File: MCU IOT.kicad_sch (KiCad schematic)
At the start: 0 parts

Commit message: Add IOT Part
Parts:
- added C?: 10nF, Capacitor_SMD:C_0603_1608Metric_Pad1.08x0.95mm_HandSolder, symbol Device:C_Small
- added C? (x8): 100nF, Capacitor_SMD:C_0603_1608Metric_Pad1.08x0.95mm_HandSolder, symbol Device:C_Small
- added D? (x5): 3.3V, Package_TO_SOT_SMD:SOT-363_SC-70-6, symbol Power_Protection:PESD3V3L5UY
- added D? (x4): 3.3V, Diode_SMD:D_SOD-123F, symbol Device:D_Zener_Small
- added D?: 5V, Diode_SMD:D_SMB, symbol Device:D_Zener_Small
- added F?: 1.75A, Fuse:Fuse_0603_1608Metric, symbol Device:Fuse_Small
- added J? (x3): *, Connector_JST:JST_PH_S6B-PH-SM4-TB_1x06-1MP_P2.00mm_Horizontal, symbol Connector_Generic_MountingPin:Conn_01x06_MountingPin
- added J?: *, Connector_USB:USB_B_Amphenol_MUSB-D511_Vertical_Rugged, symbol Connector:USB_B_Micro
- added J?: *, TerminalBlock_Phoenix:TerminalBlock_Phoenix_MPT-0,5-4-2.54_1x04_P2.54mm_Horizontal, symbol Connector:Screw_Terminal_01x04
- added J?: *, Connector_JST:JST_PH_S4B-PH-SM4-TB_1x04-1MP_P2.00mm_Horizontal, symbol Connector_Generic_MountingPin:Conn_01x04_MountingPin
- added J?: *, TerminalBlock_Phoenix:TerminalBlock_Phoenix_MPT-0,5-6-2.54_1x06_P2.54mm_Horizontal, symbol Connector:Screw_Terminal_01x06
- added R? (x3): 10k, Resistor_SMD:R_0603_1608Metric_Pad0.98x0.95mm_HandSolder, symbol Device:R_Small
- added R? (x4): 22R, Resistor_SMD:R_0805_2012Metric_Pad1.20x1.40mm_HandSolder, symbol Device:R_Small
- added R? (x3): 4.7k, Resistor_SMD:R_0603_1608Metric_Pad0.98x0.95mm_HandSolder, symbol Device:R_Small
- added R? (x2): 604R, Resistor_SMD:R_0603_1608Metric_Pad0.98x0.95mm_HandSolder, symbol Device:R_Small
- added R? (x2): 22R, Resistor_SMD:R_0603_1608Metric_Pad0.98x0.95mm_HandSolder, symbol Device:R_Small
- added SW? (x2): *, Button_Switch_SMD:SW_SPST_CK_RS282G05A3, symbol Switch:SW_Push
- added U?: TJA1042T-3, Package_SO:SOIC-8_3.9x4.9mm_P1.27mm, symbol Interface_CAN_LIN:TJA1042T-3
- added U?: *, P_MCU:XCVR_ESP32-C6-WROOM-1U-N8, symbol P_MCU:ESP32-C6-WROOM-1U-N4
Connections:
- new net: D?.5 (K4), J?.5 (Pin_5), R?.1
- new net: C?.1, R?.2, R?.2
- new net: R?.1, U?.10 (IO8)
- new net: F?.1, J?.1 (VBUS)
- new net: J?.2 (D-), R?.1
- new net: J?.3 (D+), R?.1
- new net: D?.3 (K2), J?.3 (Pin_3), R?.1
- new net: D?.6 (K5), J?.6 (Pin_6), R?.1
- new net: D?.4 (K3), J?.4 (Pin_4), R?.1
- new net +3.3V: C?.1, C?.1, C?.1, C?.1, C?.1, D?.1 (K1), J?.1 (Pin_1), J?.1 (Pin_1), J?.1 (Pin_1), J?.1 (Pin_1), R?.2, R?.2, R?.2, R?.2, U?.2 (3V3), U?.5 (VIO)
- new net +5V: C?.1, D?.1 (K), F?.2, J?.1 (Pin_1), R?.2, U?.3 (VCC)
- new net BOOT: C?.1, R?.1, SW?.1, U?.15 (IO9)
- new net CAN_H: J?.3 (Pin_3), R?.1, U?.7 (CANH)
- new net CAN_L: J?.4 (Pin_4), R?.1, U?.6 (CANL)
- new net EN: C?.1, R?.1, SW?.1, U?.3 (EN)
- new net ESP_CAN_RX: U?.21 (IO23), U?.4 (RXD)
- new net ESP_CAN_STB: U?.19 (IO21), U?.8 (STB)
- new net ESP_CAN_TX: U?.1 (TXD), U?.20 (IO22)
- new net ESP_I2C_SCL: J?.4 (Pin_4), R?.1, U?.5 (IO5)
- new net ESP_I2C_SDA: J?.3 (Pin_3), R?.1, U?.4 (IO4)
- new net ESP_PWM/ADC1: D?.1 (K), R?.2, U?.8 (IO0)
- new net ESP_PWM/ADC2: D?.1 (K), R?.2, U?.9 (IO1)
- new net ESP_PWM/ADC3: D?.1 (K), R?.2, U?.27 (IO2)
- new net ESP_PWM/ADC4: D?.1 (K), R?.2, U?.26 (IO3)
- new net ESP_SPARE1: U?.23 (IO15)
- new net ESP_SPARE2: U?.12 (IO11)
- new net ESP_SPARE3: U?.11 (IO10)
- new net ESP_SPI_CS0: J?.6 (Pin_6), U?.17 (IO19)
- new net ESP_SPI_CS1: J?.6 (Pin_6), U?.18 (IO20)
- new net ESP_SPI_MISO: J?.5 (Pin_5), J?.5 (Pin_5), U?.16 (IO18)
- new net ESP_SPI_MOSI: J?.4 (Pin_4), J?.4 (Pin_4), U?.7 (IO7)
- new net ESP_SPI_SCK: J?.3 (Pin_3), J?.3 (Pin_3), U?.6 (IO6)
- new net ESP_USB_D+: R?.1, R?.2, U?.14 (IO13)
- new net ESP_USB_D-: R?.2, U?.13 (IO12)
- new net GND: C?.2, C?.2, C?.2, C?.2, C?.2, C?.2, C?.2, C?.2, C?.2, D?.2 (A), D?.2 (A), D?.2 (A), D?.2 (A), D?.2 (A), D?.2 (A), J?.2 (Pin_2), J?.2 (Pin_2), J?.2 (Pin_2), J?.2 (Pin_2), J?.2 (Pin_2), J?.5 (GND), J?.MP (MountPin), J?.MP (MountPin), J?.MP (MountPin), J?.SH (Shield), R?.2, SW?.2, SW?.2, U?.1 (GND), U?.2 (GND), U?.28 (GND), U?.29_1 (GND), U?.29_2 (GND), U?.29_3 (GND), U?.29_4 (GND), U?.29_5 (GND), U?.29_6 (GND), U?.29_7 (GND), U?.29_8 (GND), U?.29_9 (GND)
- new net UART1_MCU_RX: U?.25 (TXD0/GPIO16)
- new net UART1_MCU_TX: U?.24 (RXD0/GPIO17)
- no-connect marks 0 -> 1
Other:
- note added: "BUS"
- note added: "CAN"
- note added: "ESP I2C"
- note added: "ESP SPI"
- note added: "Microcontroller"
- note added: "SPARE CONNECTOR"
- note added: "USB"

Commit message: IoT part finalization
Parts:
- removed J?: *, TerminalBlock_Phoenix:TerminalBlock_Phoenix_MPT-0,5-6-2.54_1x06_P2.54mm_Horizontal, symbol Connector:Screw_Terminal_01x06
- added C? (x3): 100nF, Capacitor_SMD:C_0603_1608Metric_Pad1.08x0.95mm_HandSolder, symbol Device:C_Small
- added J?: *, Connector_Molex:Molex_Micro-Fit_3.0_43045-0612_2x03_P3.00mm_Vertical, symbol Connector_Generic:Conn_02x03_Odd_Even
- J?: Comment ESP PWM / ADC -> ESP IO
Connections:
- net +3.3V: now also C?.1, J?.2 (Pin_2)
- net +5V: now also C?.1, C?.1, J?.4 (Pin_4)
- net ESP_SPARE1: now also U?.11 (IO10), J?.1 (Pin_1); no longer U?.23 (IO15)
- net ESP_SPARE2: now also J?.3 (Pin_3)
- net ESP_SPARE3: now also U?.23 (IO15), J?.5 (Pin_5); no longer U?.11 (IO10)
- net GND: now also J?.MP (MountPin), C?.2, C?.2, C?.2, J?.6 (Pin_6)
- net ESP_PWM/ADC1 renamed ESP_IO0
- net ESP_PWM/ADC2 renamed ESP_IO1
- net ESP_PWM/ADC3 renamed ESP_IO2
- net ESP_PWM/ADC4 renamed ESP_IO3
- net UART1_MCU_RX renamed IOT_UART_MCU_RX
- net UART1_MCU_TX renamed IOT_UART_MCU_TX
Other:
- note added: "ESP IO"
- note added: "ESP SPARE CONNECTOR"
- note removed: "SPARE CONNECTOR"
- moved on the sheet: C?, D?, D?A, D?B, D?C, D?D, D?E, J?, R?

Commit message: IOT part Finilization
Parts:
- U?: value TJA1042T-3 -> *; Comment (none) -> CAN Transceiver; Manufacturer (none) -> NXP; PackageReference (none) -> SOIC-8_3.9x4.9mm_P1.27mm; PartNumber (none) -> TJA1042BT
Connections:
- net ESP_SPARE1: now also U?.12 (IO11); no longer U?.11 (IO10)
- net ESP_SPARE2: now also U?.23 (IO15); no longer U?.12 (IO11)
- net BOOT renamed ESP_BOOT0
- net ESP_SPARE3: no longer names the net of J?.5 (Pin_5)
- net ESP_SPARE3: no longer U?.23 (IO15)
- new net MCU_BOOT0: U?.11 (IO10)
- no-connect marks 1 -> 2
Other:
- note added: "ESP USB"
- note removed: "USB"
- moved on the sheet: C?, D?A, J?, R?, U?

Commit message: Release Schematic REV A-01
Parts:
- removed C?: 100nF, Capacitor_SMD:C_0603_1608Metric_Pad1.08x0.95mm_HandSolder, symbol Device:C_Small
- removed J?: *, Connector_JST:JST_PH_S6B-PH-SM4-TB_1x06-1MP_P2.00mm_Horizontal, symbol Connector_Generic_MountingPin:Conn_01x06_MountingPin
- J28: renamed from J?; Comment SPI2 -> SPI1
- gave numbers to parts that had none: 41
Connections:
- net ESP_SPI_CS0: no longer J28.6 (Pin_6)
- net ESP_SPI_CS1: now also J28.6 (Pin_6)
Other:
- company: Blue Signal -> Nexvantis

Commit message: Release Schematic REV A-01
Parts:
- removed J33: *, Connector_Molex:Molex_Micro-Fit_3.0_43045-0612_2x03_P3.00mm_Vertical, symbol Connector_Generic:Conn_02x03_Odd_Even
- added J?: Conn_02x02_Counter_Clockwise, Connector_Molex:Molex_Micro-Fit_3.0_43045-0412_2x02_P3.00mm_Vertical, symbol Connector_Generic:Conn_02x02_Counter_Clockwise
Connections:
- net ESP_SPARE2 is gone; now on net MicroSD_Detection: U10.23 (IO15)
- net +3.3V: now also J?.4 (Pin_4)
- net +5V: now also J?.3 (Pin_3)
- net ESP_SPARE1: now also J?.1 (Pin_1)
- net GND: now also J?.2 (Pin_2)
- no-connect marks 2 -> 1
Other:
- moved on the sheet: R77, U10

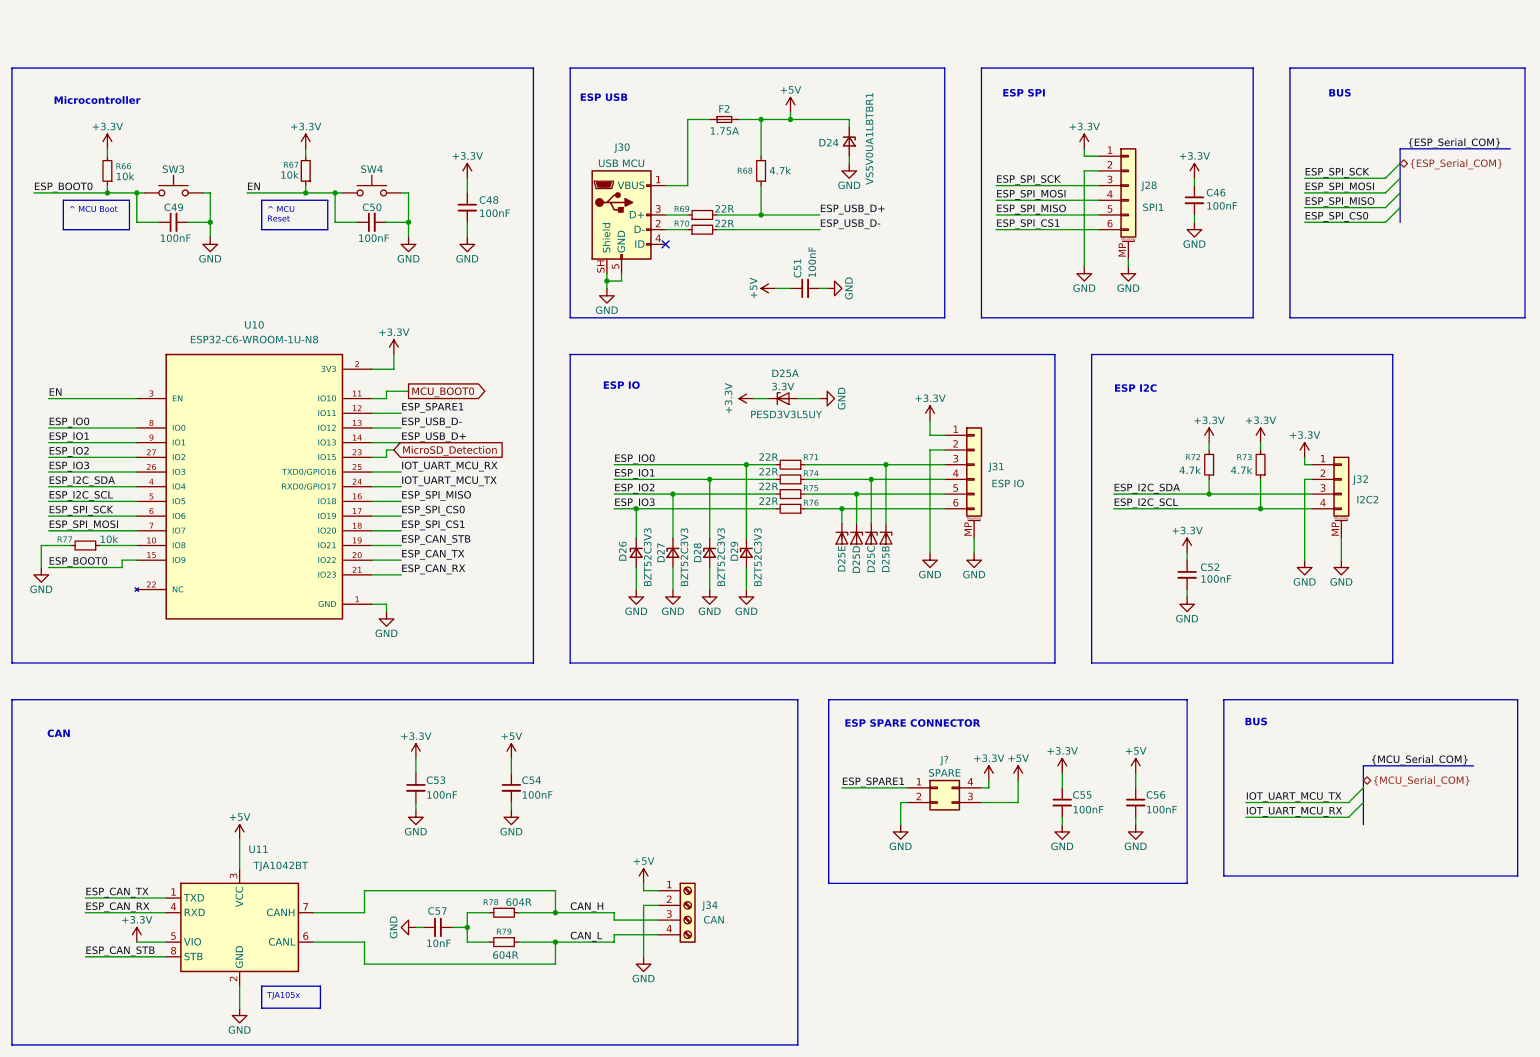
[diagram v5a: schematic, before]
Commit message: [Project][Added] CI/CD environment
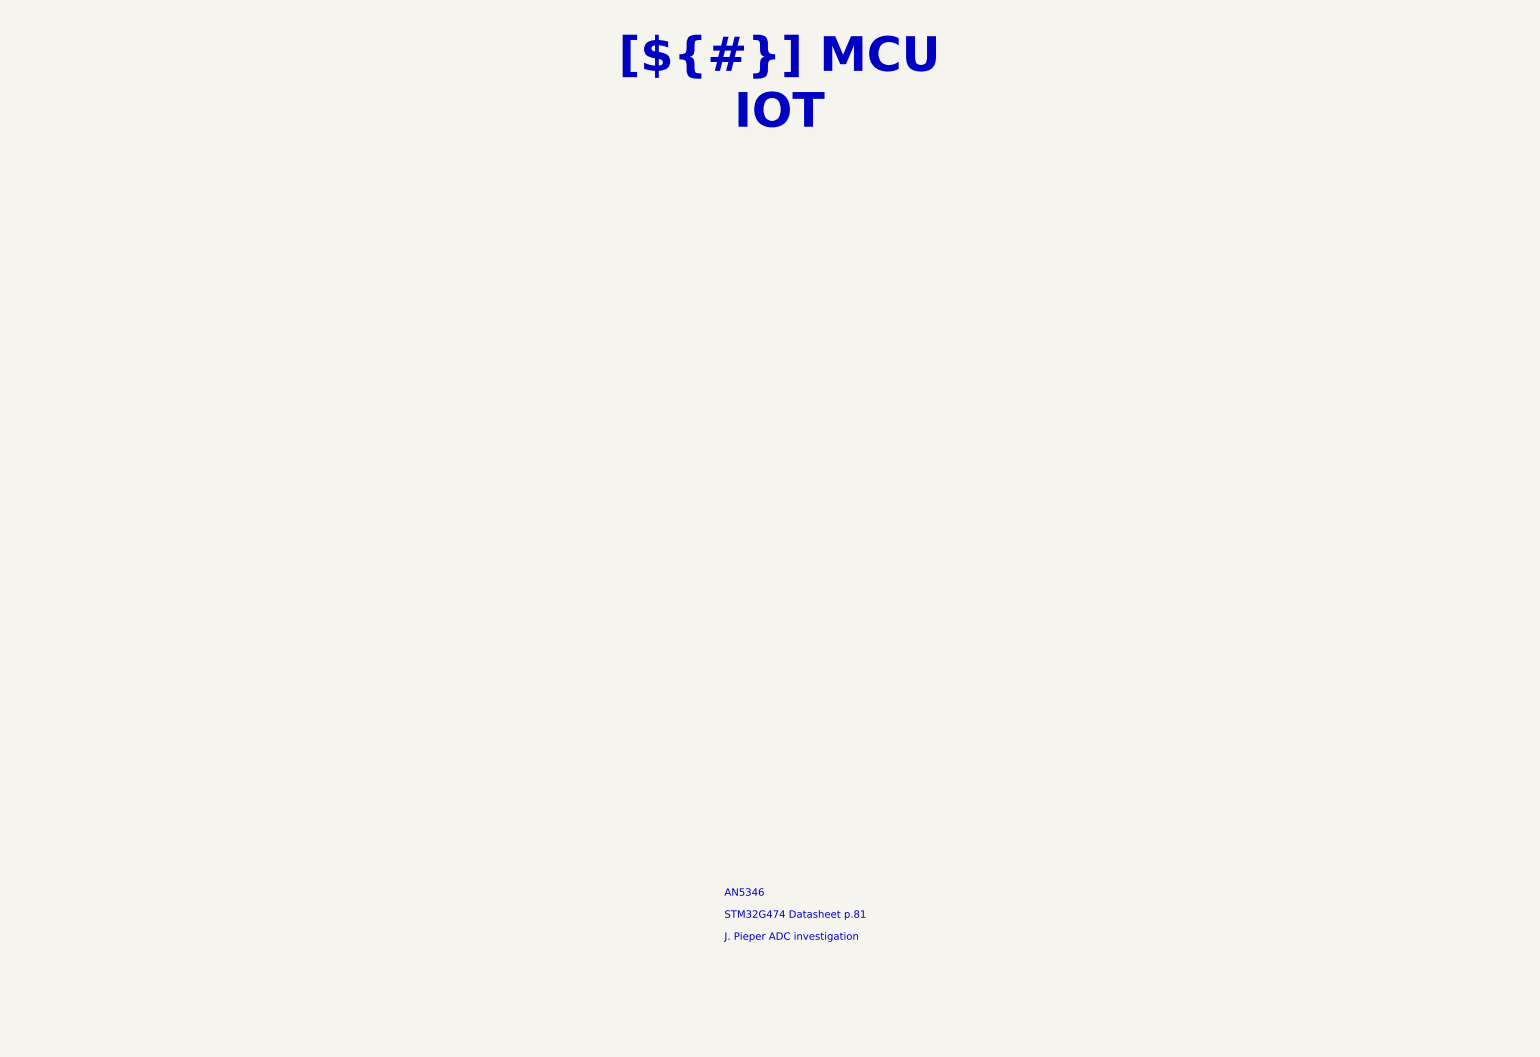
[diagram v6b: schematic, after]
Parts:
- removed C46, C48, C49, C50, C51, C52, C53, C54, C55, C56: 100nF, Capacitor_SMD:C_0603_1608Metric_Pad1.08x0.95mm_HandSolder, symbol Device:C_Small
- removed C57: 10nF, Capacitor_SMD:C_0603_1608Metric_Pad1.08x0.95mm_HandSolder, symbol Device:C_Small
- removed D24: 5V, Diode_SMD:D_SMB, symbol Device:D_Zener_Small
- removed D25: 3.3V, Package_TO_SOT_SMD:SOT-363_SC-70-6, symbol Power_Protection:PESD3V3L5UY
- removed D26, D27, D28, D29: 3.3V, Diode_SMD:D_SOD-123F, symbol Device:D_Zener_Small
- removed F2: 1.75A, Fuse:Fuse_0603_1608Metric, symbol Device:Fuse_Small
- removed J28, J31: *, Connector_JST:JST_PH_S6B-PH-SM4-TB_1x06-1MP_P2.00mm_Horizontal, symbol Connector_Generic_MountingPin:Conn_01x06_MountingPin
- removed J30: *, Connector_USB:USB_B_Amphenol_MUSB-D511_Vertical_Rugged, symbol Connector:USB_B_Micro
- removed J32: *, Connector_JST:JST_PH_S4B-PH-SM4-TB_1x04-1MP_P2.00mm_Horizontal, symbol Connector_Generic_MountingPin:Conn_01x04_MountingPin
- removed J34: *, TerminalBlock_Phoenix:TerminalBlock_Phoenix_MPT-0,5-4-2.54_1x04_P2.54mm_Horizontal, symbol Connector:Screw_Terminal_01x04
- removed J?: Conn_02x02_Counter_Clockwise, Connector_Molex:Molex_Micro-Fit_3.0_43045-0412_2x02_P3.00mm_Vertical, symbol Connector_Generic:Conn_02x02_Counter_Clockwise
- removed R66, R67, R77: 10k, Resistor_SMD:R_0603_1608Metric_Pad0.98x0.95mm_HandSolder, symbol Device:R_Small
- removed R68, R72, R73: 4.7k, Resistor_SMD:R_0603_1608Metric_Pad0.98x0.95mm_HandSolder, symbol Device:R_Small
- removed R69, R70: 22R, Resistor_SMD:R_0603_1608Metric_Pad0.98x0.95mm_HandSolder, symbol Device:R_Small
- removed R71, R74, R75, R76: 22R, Resistor_SMD:R_0805_2012Metric_Pad1.20x1.40mm_HandSolder, symbol Device:R_Small
- removed R78, R79: 604R, Resistor_SMD:R_0603_1608Metric_Pad0.98x0.95mm_HandSolder, symbol Device:R_Small
- removed SW3, SW4: *, Button_Switch_SMD:SW_SPST_CK_RS282G05A3, symbol Switch:SW_Push
- removed U10: *, P_MCU:XCVR_ESP32-C6-WROOM-1U-N8, symbol P_MCU:ESP32-C6-WROOM-1U-N4
- removed U11: *, Package_SO:SOIC-8_3.9x4.9mm_P1.27mm, symbol Interface_CAN_LIN:TJA1042T-3
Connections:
- no-connect marks 1 -> 0
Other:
- note added: "AN5346"
- note added: "J. Pieper ADC investigation"
- note added: "STM32G474 Datasheet p.81"
- note removed: "BUS"
- note removed: "CAN"
- note removed: "ESP I2C"
- note removed: "ESP IO"
- note removed: "ESP SPARE CONNECTOR"
- note removed: "ESP SPI"
- note removed: "ESP USB"
- note removed: "Microcontroller"
- company: Nexvantis -> ${COMPANY}
- title: Data Acquisition Board -> MCU IOT

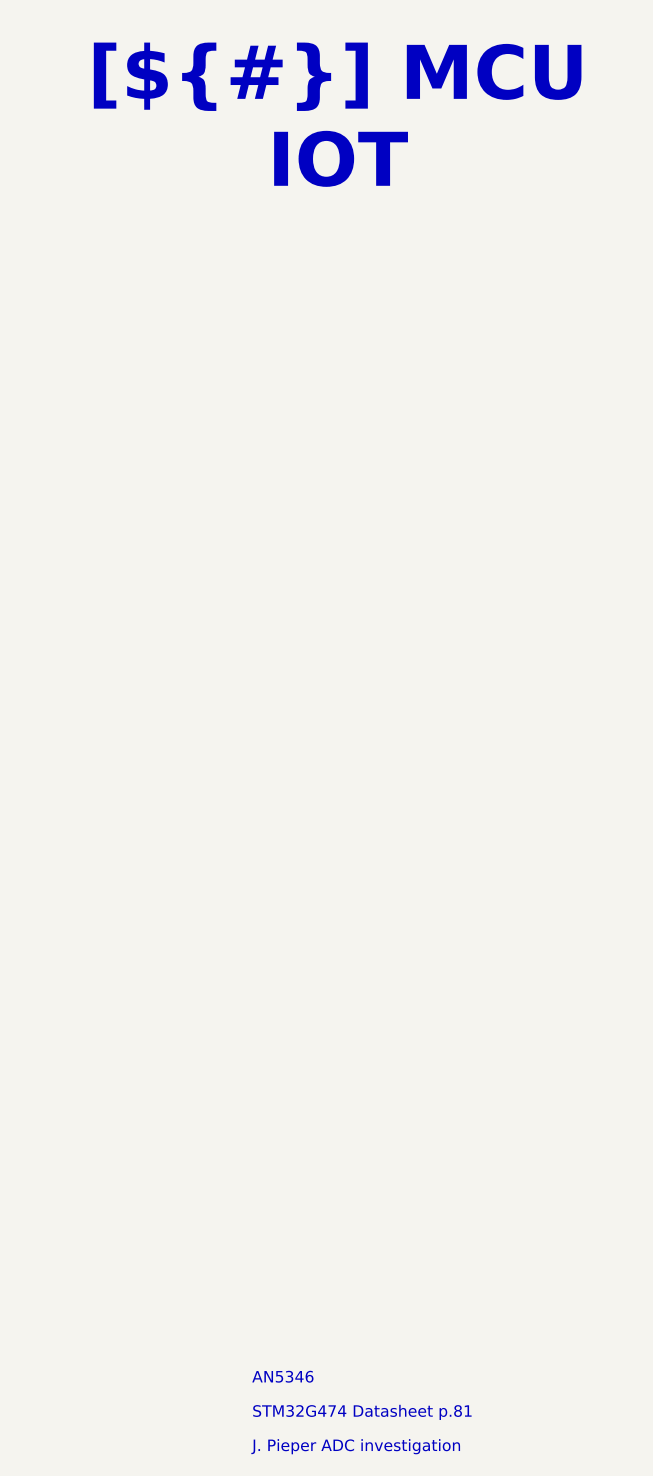
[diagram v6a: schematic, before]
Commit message: [Project][Added] CI/CD environment
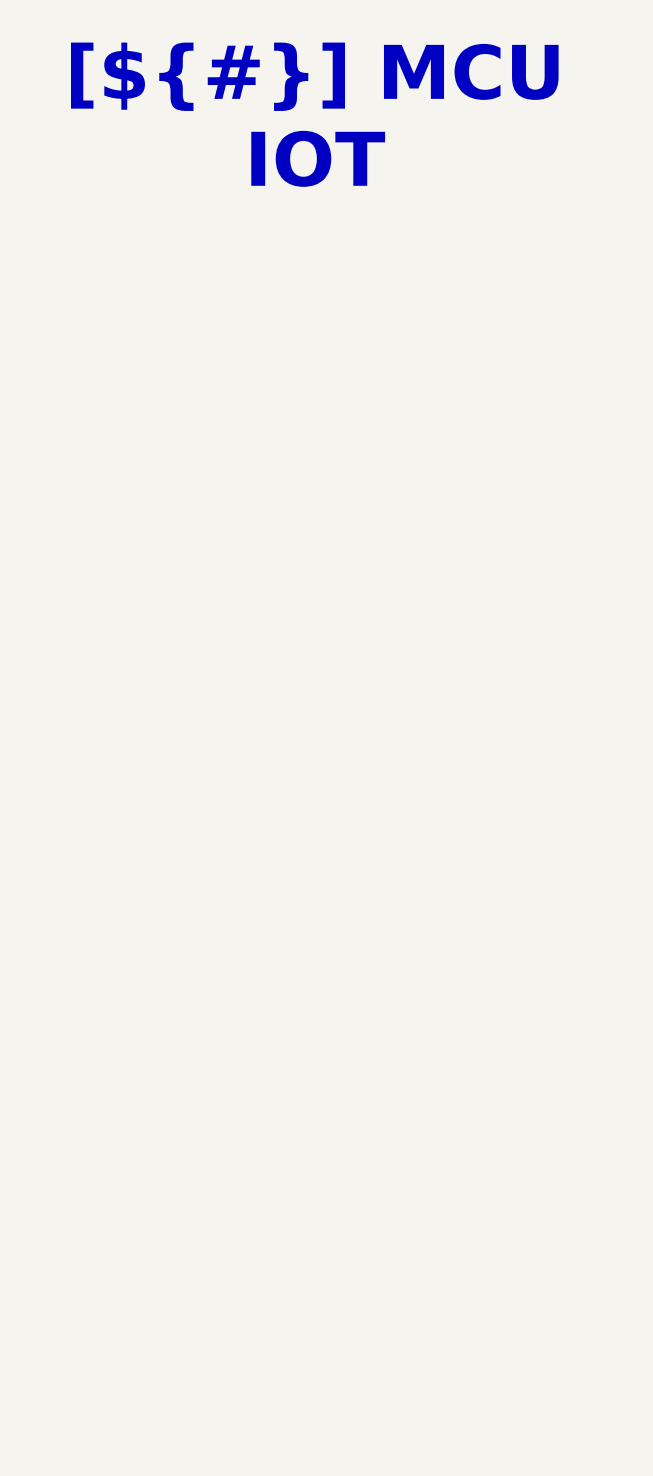
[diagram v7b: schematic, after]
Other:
- note removed: "AN5346"
- note removed: "J. Pieper ADC investigation"
- note removed: "STM32G474 Datasheet p.81"
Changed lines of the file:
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@@
 (kicad_sch
-	(version 20260306)
+	(version 20250114)
 	(generator "eeschema")
-	(generator_version "10.0")
+	(generator_version "9.0")
 	(paper "A4")
 	(title_block
@@
 		(company "${COMPANY}")
 	)
-	(text "J. Pieper ADC investigation"
-		(exclude_from_sim no)
-		(at 142.24 170.18 0)
-		(effects
-			(font
-				(face "Arial")
-				(size 1.27 1.27)
-				(color 0 0 0 1)
-			)
-			(justify left bottom)
-			(href "https://jpieper.com/2023/07/24/stm32g4-adc-performance-part-2/")
-		)
-	)
-	(text "STM32G474 Datasheet p.81"
-		(exclude_from_sim no)
-		(at 142.24 166.37 0)
-		(effects
-			(font
-				(face "Arial")
-				(size 1.27 1.27)
-				(color 0 0 0 1)
-			)
-			(justify left bottom)
-			(href "https://www.st.com/resource/en/datasheet/stm32g474cb.pdf")
-		)
-	)
-	(text "AN5346"
-		(exclude_from_sim no)
-		(at 142.24 162.56 0)
-		(effects
-			(font
-				(face "Arial")
-				(size 1.27 1.27)
-				(color 0 0 0 1)
-			)
-			(justify left bottom)
-			(href "https://www.st.com/resource/en/application_note/an5346-stm32g4-adc-use-tips-and-recommendations-stmicroelectronics.pdf")
-		)
-	)
 	(text_box "[${#}] ${TITLE}"
 		(exclude_from_sim no)
-		(at 115.57 15.24 0)
+		(at 113.03 15.24 0)
 		(size 72.39 12.7)
 		(margins 4.4999 4.4999 4.4999 4.4999)

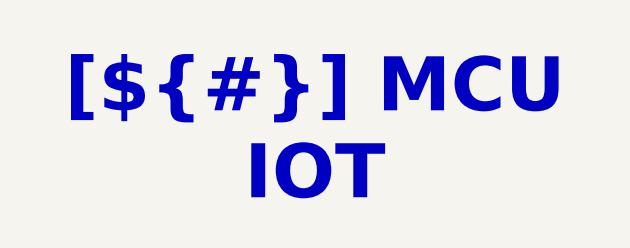
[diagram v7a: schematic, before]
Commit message: [Schematic][Add] Add of a new page : MCU Expander
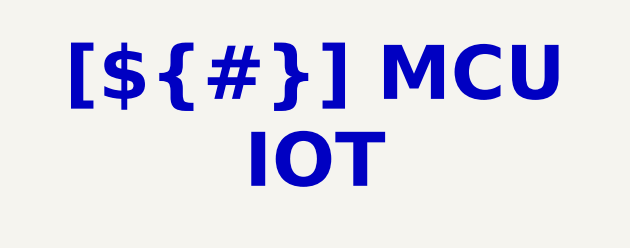
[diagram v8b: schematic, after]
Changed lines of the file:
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@@
 	(text_box "[${#}] ${TITLE}"
 		(exclude_from_sim no)
-		(at 113.03 15.24 0)
+		(at 113.03 13.97 0)
 		(size 72.39 12.7)
 		(margins 4.4999 4.4999 4.4999 4.4999)
